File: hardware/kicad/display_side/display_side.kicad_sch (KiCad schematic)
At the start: 30 parts, among them J1 RJ45, J2 EPD_FFC_24, J3 UART-DBG, J4 USB-OTG, U1 R-78E3.3-0.5, U2 SN65HVD3082E

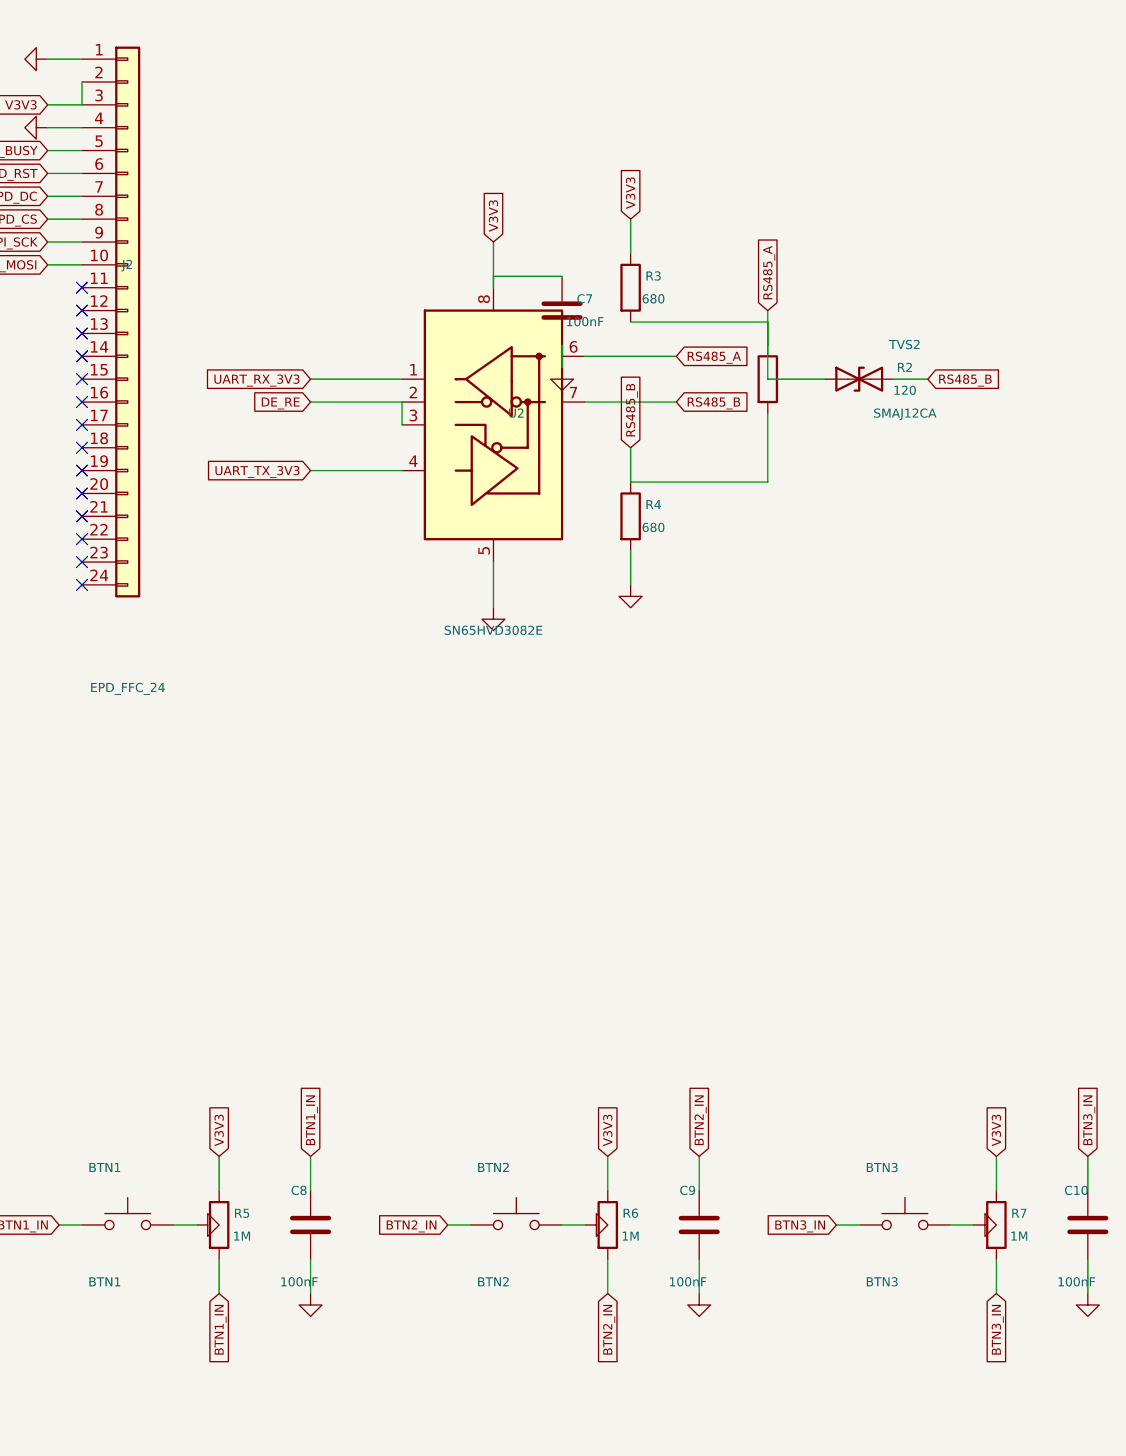
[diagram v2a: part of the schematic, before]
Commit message: hardware: CP6 iter-11 — comprehensive geometry audit + build-time gate; fix body-on-body overlaps
The iter-10 detector found label-flag overlaps but was blind to
SYMBOL-vs-SYMBOL collisions: a GND power-port ground-triangle glyph was
sitting on top of resistors R5/R6/R7, and the RS-485 decoupling caps
(C7/C10) grazed the tall transceiver chip body — all with zero text
overlap, so both prior audits reported clean while the render was
clearly cluttered (user-flagged).

Root cause (systemic): piecemeal pair-type checks always leave a blind
spot. Fix: make the audit comprehensive and gate the build on it.

label_body_audit.py — now a complete geometric collision audit:
- adds body∩body (MIN 0.5 mm² — two glyphs must never share ink) and
  flag∩flag, alongside the existing flag∩body and flag∩ref/value.
- recalibrated flag bbox thickness (half_t = TEXT_H/2 + 0.25) so it
  stays under the 2.54 mm pin pitch — adjacent connector-pin labels no
  longer false-positive as flag∩flag.
- exits non-zero on any finding.

build_schematics.py — new run_readability_audits() gate:
- runs BOTH audits (strict text + comprehensive geometry) on both
  boards at the end of every build, prints per-board PASS/FAIL, and
  raises SystemExit on any finding. Every regeneration now self-checks;
  a fix that creates a new overlap fails the build (the loop).

Layout fixes (both boards now 0 findings on both audits, ERC 0/0):
- BTN debounce GND ports routed DOWN (apex-down, below the switch)
  instead of toward the pull-up R to their right.
- RS-485 decoupling caps C7 (display) / C10 (battery) lifted fully
  above the tall chip body, GND port pointing up, away from the body.

Codified in project files (not just memory):
- DESIGNER.md §0 checklist item 5 now requires BOTH audits + the gate,
  plus the high-DPI per-region inspection rule.
- REVIEWER.md §4 D16 list requires both audits; text-only PASS is a
  finding.
- decisions.md D16: new "Second failure" teaching example (the audit's
  own blind spot)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
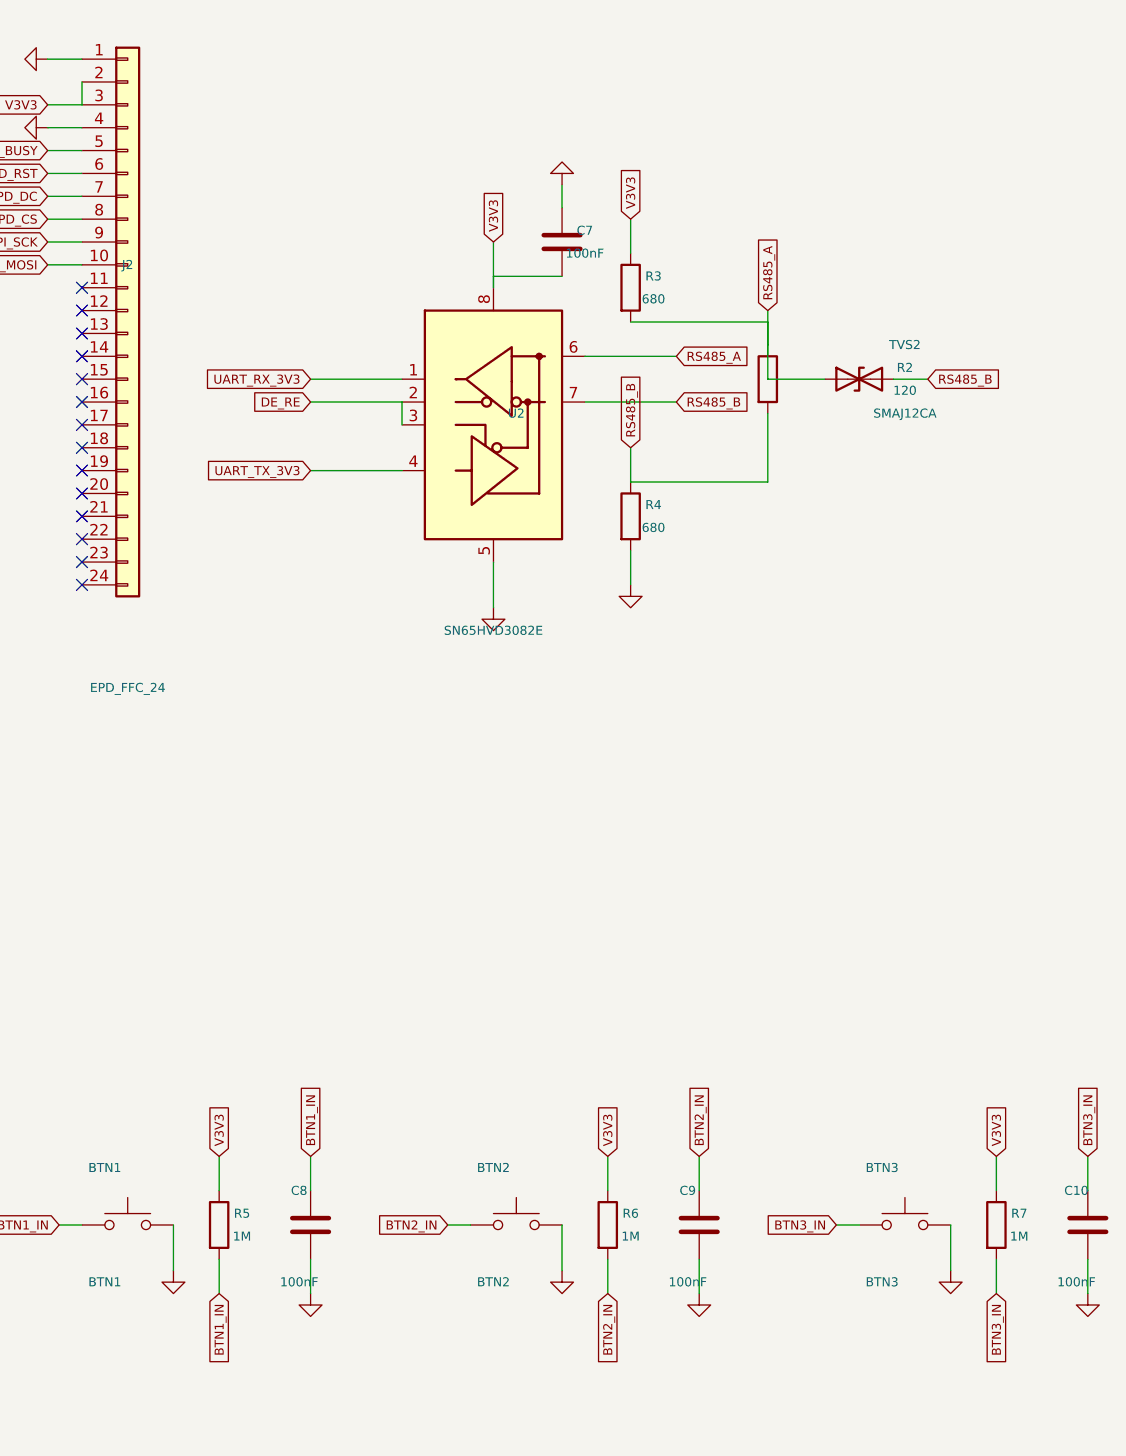
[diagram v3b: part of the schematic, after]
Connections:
- net GND: now also C7.1; no longer C7.2
- net V3V3: now also C7.2; no longer C7.1

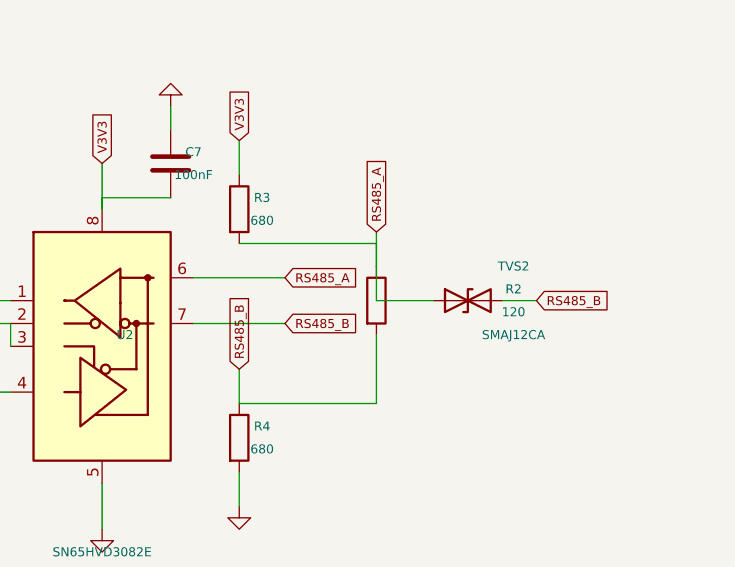
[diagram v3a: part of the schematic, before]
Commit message: hardware: CP6 iter-12 — wire-aware audit, thicker net lines, wiring-discipline guidelines
Per user feedback (2026-06-16): expand the overlap audit to all
element classes incl. wires; make net lines thicker; adopt three
wiring-discipline guidelines (wire nearby same-net labels; wire
datasheet parts into IC blocks; minimise/clarify crossings).

label_body_audit.py — wire is now a first-class element:
- wire∩body: a wire run through/into a component body (a pin
  connection at the edge clips ~0; a stub routed into the interior or
  a pass-through is flagged). Power-port/flag terminals only flag true
  pass-throughs (a wire always legitimately ends at them).
- wire∩flag-core: a wire crossing a flag's TEXT body (strike-through),
  with the ~2.5 mm chevron/connection zone excluded so a normal pin
  connection at the chevron tip does not false-trigger.
- wire∩text: a wire through ref/value text.
- advisories: same-net GlobalLabel pairs within ~20 mm (guideline a)
  and the free wire-crossing count (guideline c).
- dropped the "T-tap without junction" check — KiCad auto-renders
  junction dots at endpoint-to-wire taps, so it was a false positive.
- flag bbox thickness calibrated under the 2.54 mm pitch so adjacent
  connector-pin labels do not false-trigger as flag∩flag.

build_schematics.py:
- WIRE_WIDTH = 0.254 mm (10 mil) net-line stroke (KiCad's 6 mil
  default is faint); applied in _place_wire.
- RS485_A trunk (R2 display / R10 battery) rerouted AROUND the
  resistor body instead of straight down through it (wire∩body fix).
- audit gate reports PASS/FAIL but no longer aborts the build, so
  iteration is possible while findings remain.

Codified guidelines a/b/c + the wire-audit classes in DESIGNER.md §0,
REVIEWER.md §4, decisions.md D16 portability, and memory.

State: ERC 0/0 both boards; text-overlap 0; body∩body 0; net lines
thicker. KNOWN REMAINING (tracked, needs deliberate cluster reflow —
rushed label nudges break ERC with dangling wires): 3 wire∩flag
strike-thr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
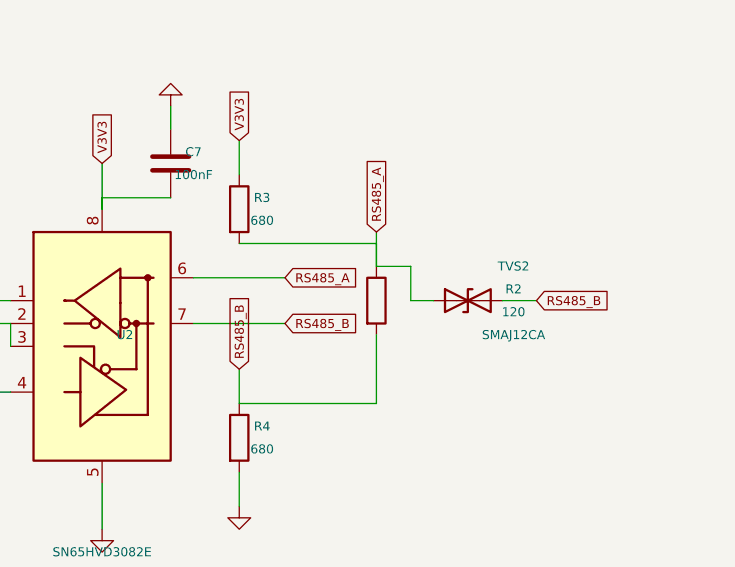
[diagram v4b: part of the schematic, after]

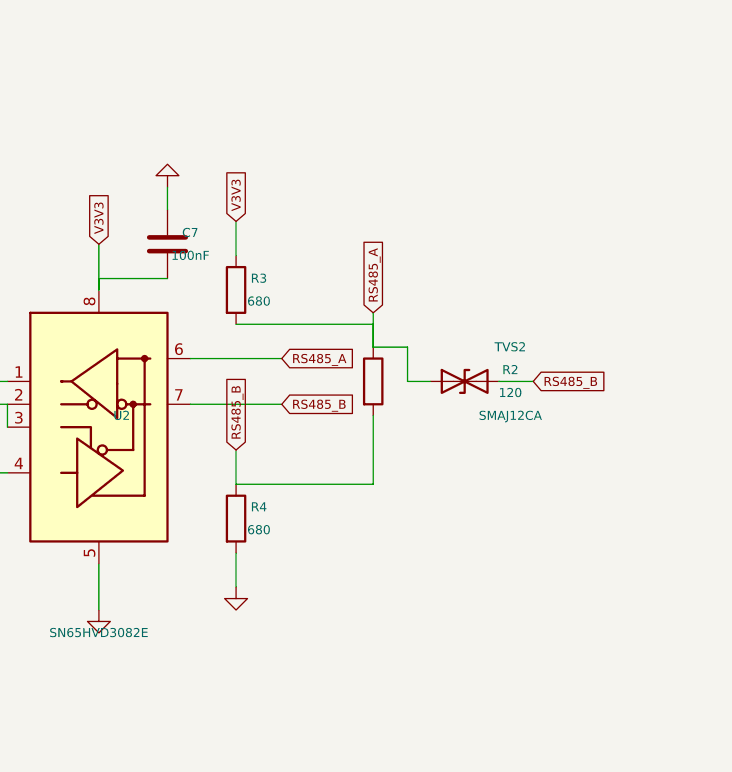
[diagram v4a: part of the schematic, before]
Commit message: hardware: CP6 iter-13 — RS-485 two-rail termination reflow; all overlaps zero, gate enforced
Dedicated reflow of the dense RS-485 clusters (guidelines a/b) plus the
buck-SW node, clearing the last wire∩flag strike-throughs. Both boards
now pass the full audit gate (0 text + 0 geometry findings) AND ERC 0/0.

New helper _place_rs485_term_block() — a clean two-rail termination
block used identically on both boards:
- A/B differential lines are two horizontal rails 6 G apart (pin-6 = A;
  pin-7 jogs down to B), drawn as SEGMENTS between consecutive tap
  points so every pin taps at a shared wire endpoint (KiCad only
  auto-connects pins to wires at endpoints, not mid-span).
- 120 Ω termination + SMAJ12CA TVS bridge the rails vertically; the two
  680 Ω bias resistors tap up→VCC / down→GND; ONE RS485_A and ONE
  RS485_B label per rail carry the net cross-sheet.
This wires every datasheet part into the chip's block and removes the
per-part RS485_A/B flag forest — eliminating the pin-7-wire-through-R4/
R12-flag strike-throughs and the same-net-label advisories.

_place_symbol(): fields on a rotated symbol now counter-rotate by
-angle (KiCad composes field angle with symbol angle) and a new
autoplace_fields=False keeps hand-tuned ref/value from being re-stacked
on a rotated body — needed for the angle-90 TVS.

U1_SW (buck internal node): dropped the flag the SW→L1 wire struck
through; the net name now sits on a short down-stub off pin 5 (pin
stays connected; the node is otherwise defined by its wires).

Audit gate restored to HARD-FAIL (raises on any text/geometry finding)
now that both boards are at zero, so future regressions fail the build.

Memory updated with the two-rail idiom + the two KiCad gotchas
(segment rails for endpoint connections; counter-rotate rotated-symbol
fields).

Co-Authored-By: Claude Opus 4.7 (1M context) <noreply@anthropic.com>
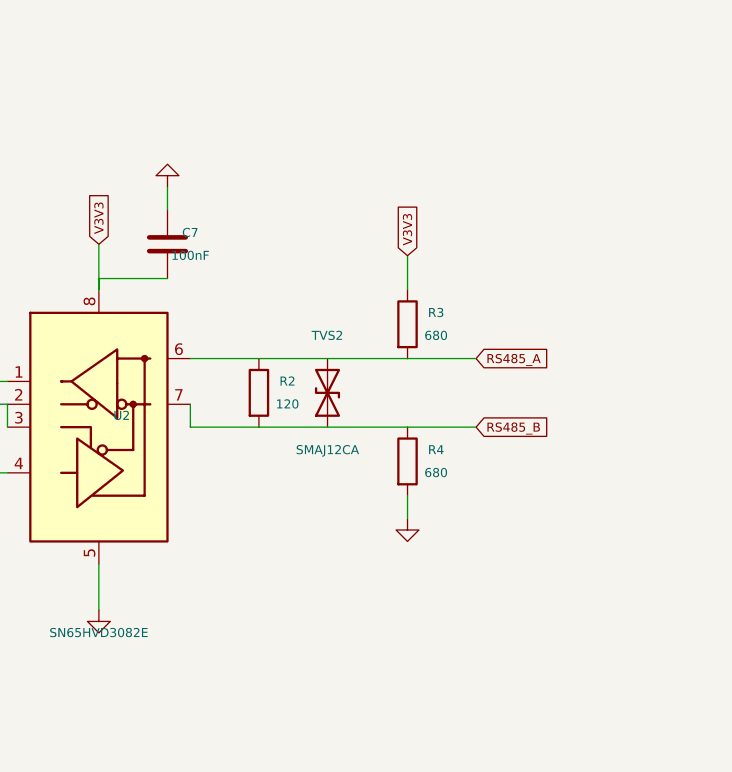
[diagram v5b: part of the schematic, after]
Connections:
- net RS485_A: now also TVS2.2 (A2); no longer TVS2.1 (A1)
- net RS485_B: now also TVS2.1 (A1); no longer TVS2.2 (A2)

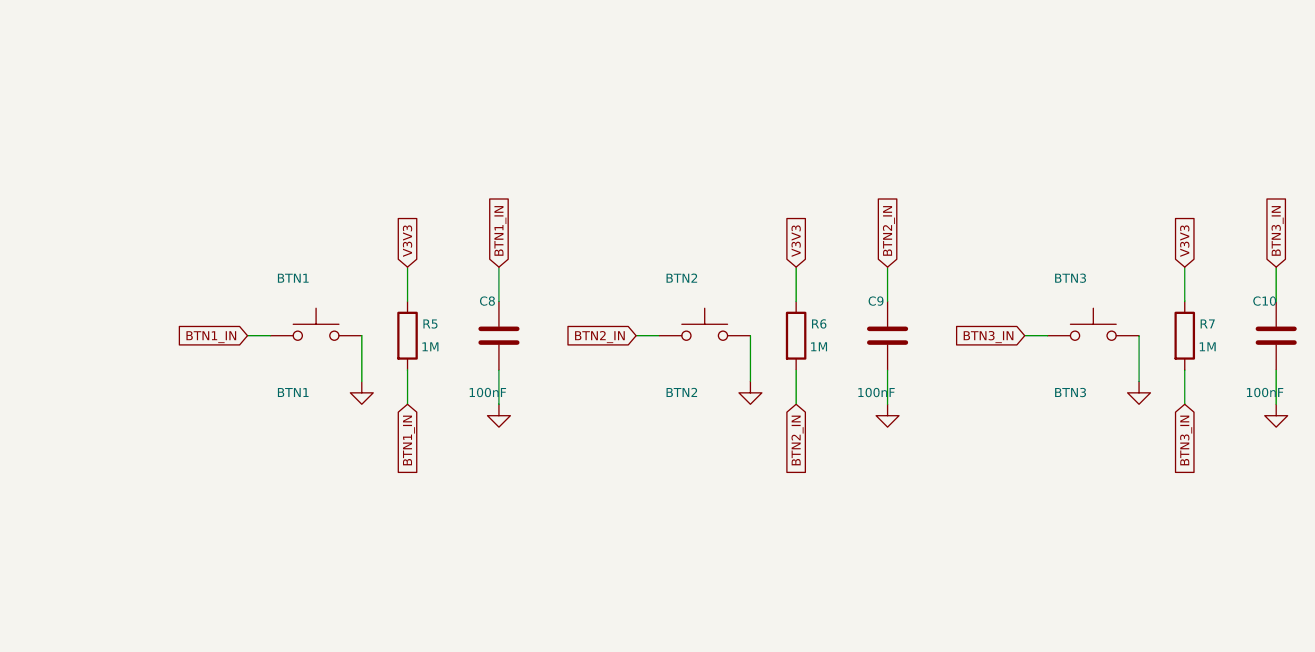
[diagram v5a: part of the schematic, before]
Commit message: hardware: CP6 iter-14 — display BTN debounce blocks wired (guideline b)
Each of the 3 buttons is now one wired debounce block (switch + 1MΩ
pull-up + 100nF) with a single BTN<N>_IN label to the MCU, via new
_place_btn_debounce() helper. Was 3 same-net BTN<N>_IN flags per button
(6 same-net advisories). ERC 0/0, audit gate PASS on both boards.

Co-Authored-By: Claude Opus 4.7 (1M context) <noreply@anthropic.com>
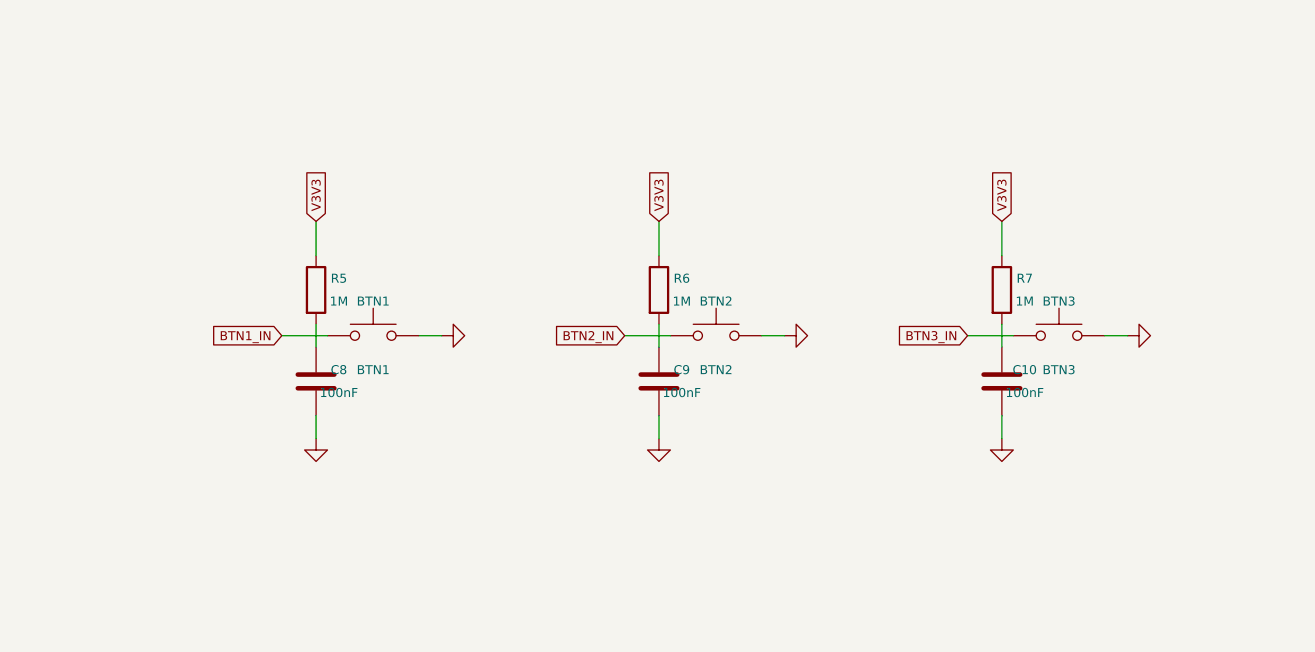
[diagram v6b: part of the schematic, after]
